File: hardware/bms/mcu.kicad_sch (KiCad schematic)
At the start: 34 parts

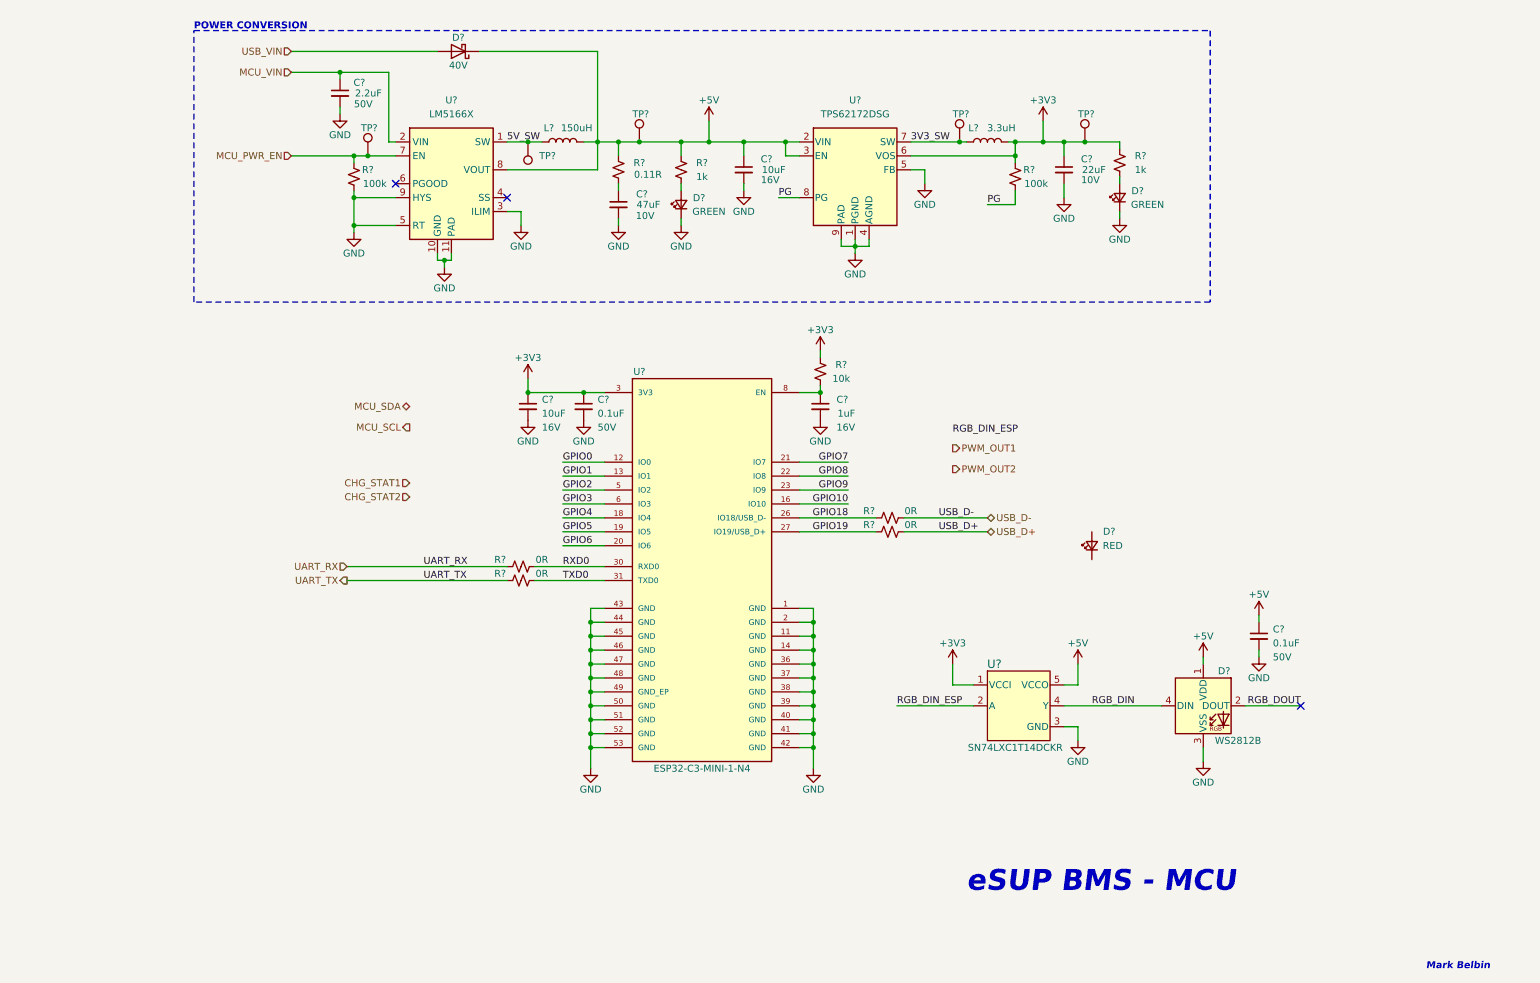
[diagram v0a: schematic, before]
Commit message: Sch mostly complete! Just have the USB C connector left to sort out.
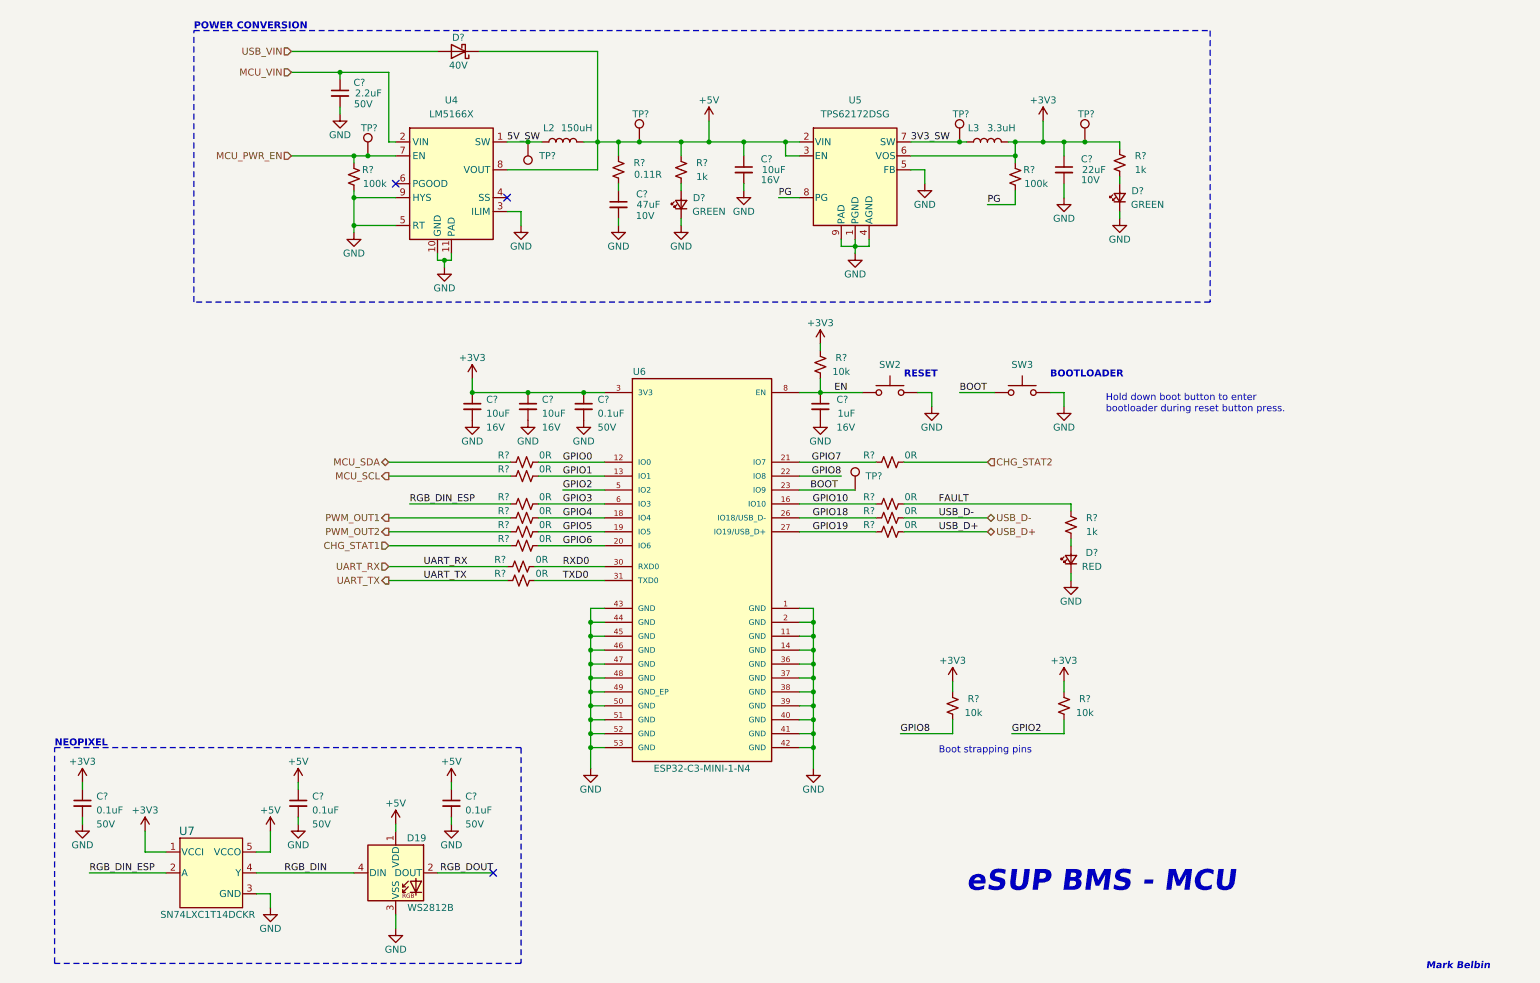
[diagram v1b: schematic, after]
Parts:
- added C? (x2): 0.1uF, Capacitor_SMD:C_0603_1608Metric, symbol Device:C_Small
- added C?: 10uF, Capacitor_SMD:C_0603_1608Metric, symbol Device:C_Small
- added R? (x2): 10k, Resistor_SMD:R_0603_1608Metric, symbol Device:R_Small_US
- added R? (x8): 0R, Resistor_SMD:R_0603_1608Metric, symbol Device:R_Small_US
- added R?: 1k, Resistor_SMD:R_0603_1608Metric, symbol Device:R_Small_US
- added SW2, SW3: SW_Push, bms:SW_B3U-1000P, symbol Switch:SW_Push
- added TP?: TestPoint, TestPoint:TestPoint_Pad_D1.0mm, symbol Connector:TestPoint
- L3: renamed from L?; footprint (none) -> Inductor_SMD:L_1008_2520Metric; Current (none) -> 1.2A; DCR (none) -> 125m; MFG (none) -> Murata Electronics; MFG PN (none) -> LQM2HPN3R3MG0L
- gave numbers to parts that had none: 6
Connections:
- net +3V3: now also C?.1, C?.1, R?.1, R?.1
- net +5V: now also C?.1
- net CHG_STAT1: now also R?.1
- net CHG_STAT2: now also R?.2
- net GND: now also D?.1 (K), C?.2, C?.2, C?.2, SW2.2, SW3.2
- net GPIO0: now also R?.2
- net GPIO1: now also R?.2
- net GPIO10: now also R?.1
- net GPIO2: now also R?.2
- net GPIO3: now also R?.2
- net GPIO4: now also R?.2
- net GPIO5: now also R?.2
- net GPIO6: now also R?.2
- net GPIO7: now also R?.1
- net GPIO8: now also R?.2
- net MCU_SCL: now also R?.1
- net MCU_SDA: now also R?.1
- net PWM_OUT1: now also R?.1
- net PWM_OUT2: now also R?.1
- net RGB_DIN_ESP: now also R?.1
- net at D?.2 (A): now also R?.1
- net EN: now reaches C?.1, R?.2, U6.8 (EN)
- net EN: now also SW2.1
- net GPIO9 renamed BOOT
- net BOOT: now also SW3.1, TP?.1
- new net FAULT: R?.2, R?.2
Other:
- note added: "BOOTLOADER"
- note added: "Boot strapping pins"
- note added: "Hold down boot button to enter bootloader during reset button press."
- note added: "NEOPIXEL"
- note added: "RESET"
- title: (none) -> eSUP - ESP32 MCU
- moved on the sheet: C?, D19, D?, R?, U7

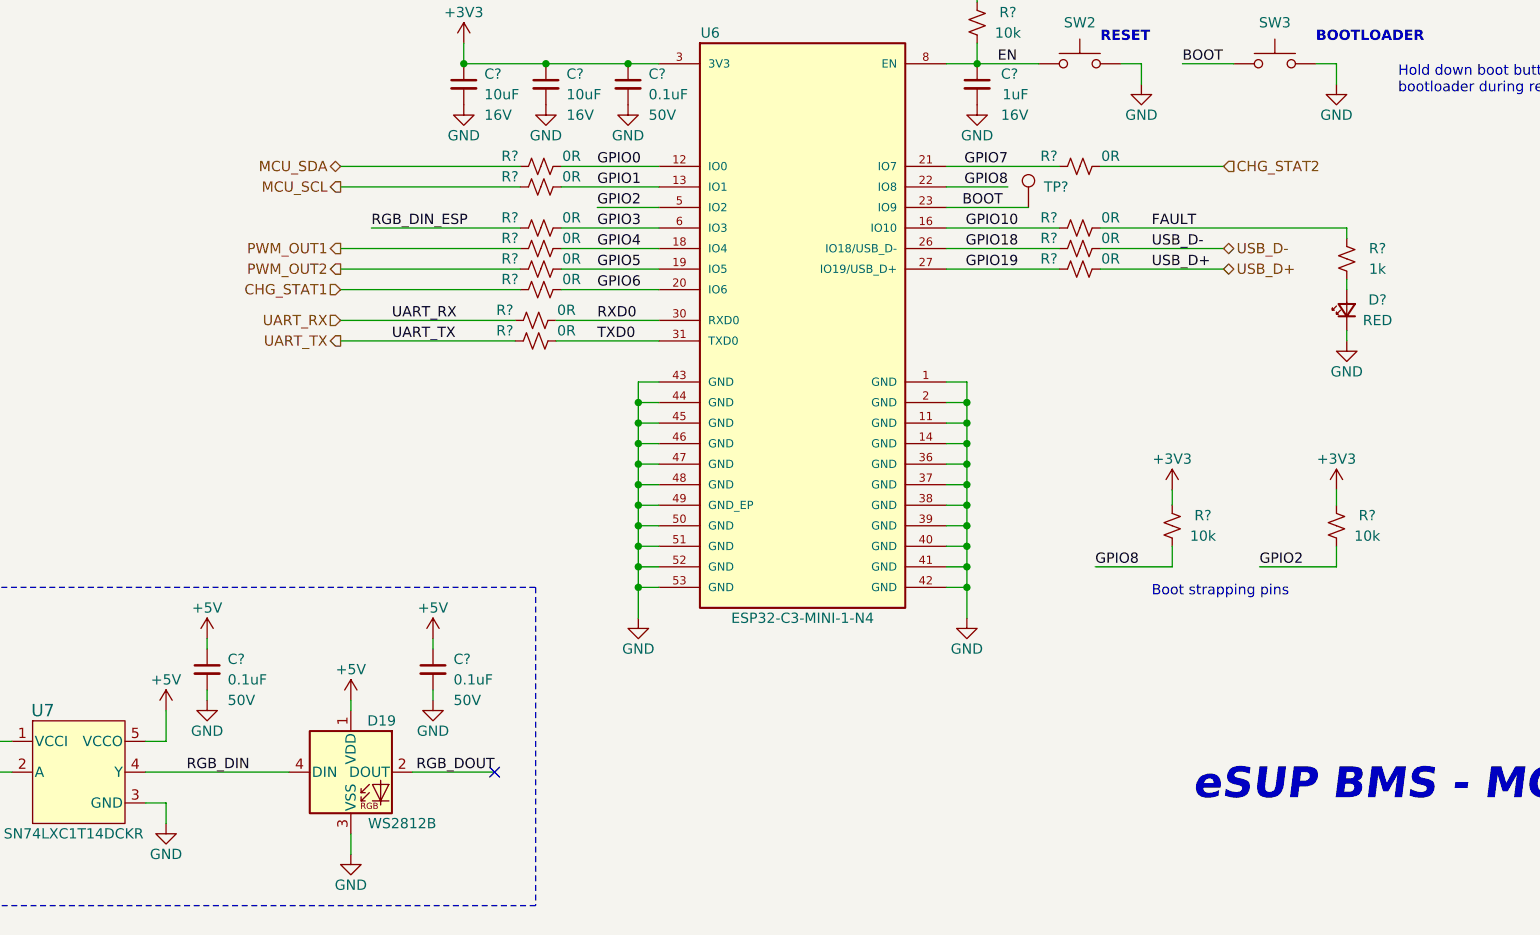
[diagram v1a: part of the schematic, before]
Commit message: Updated USB C connector, fixed all sch ERC errors, imported footprints into pcb file, fixed any pcb import errors.
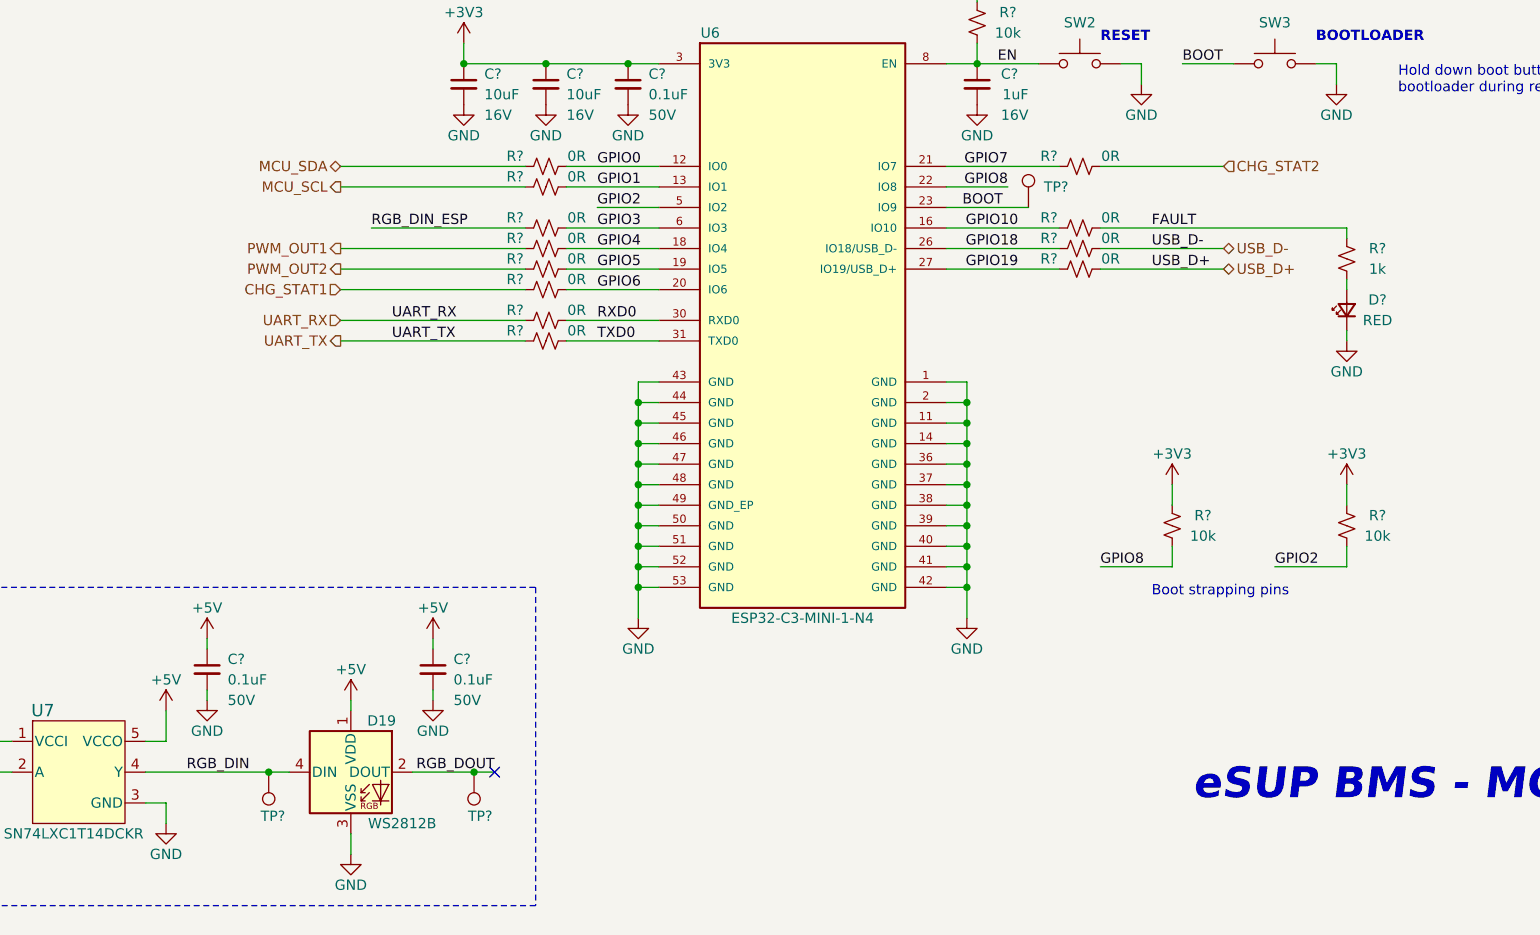
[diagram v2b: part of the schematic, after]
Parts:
- added TP? (x2): TestPoint, TestPoint:TestPoint_Pad_D1.0mm, symbol Connector:TestPoint
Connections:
- net RGB_DIN: now also TP?.1
- net RGB_DOUT: now also TP?.1
- now unconnected: U6.10 (NC), U6.15 (NC), U6.17 (NC), U6.24 (NC), U6.25 (NC), U6.28 (NC), U6.29 (NC), U6.32 (NC), U6.33 (NC), U6.34 (NC), U6.35 (NC), U6.4 (NC), U6.7 (NC), U6.9 (NC)
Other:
- moved on the sheet: R?

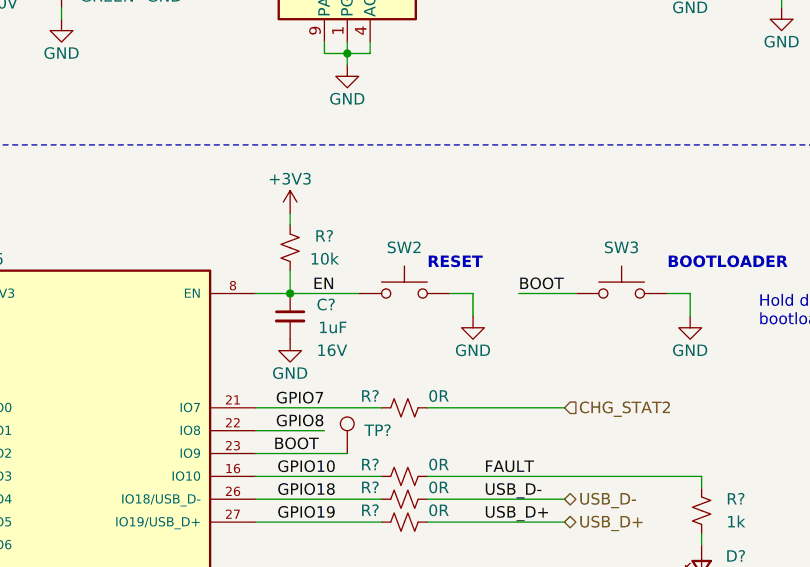
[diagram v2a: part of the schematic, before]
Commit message: Sch cleanup, added extra netties
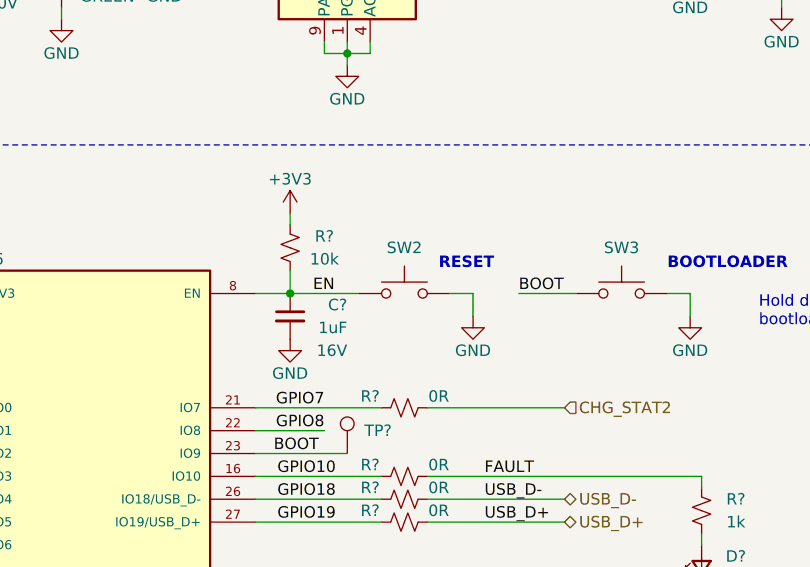
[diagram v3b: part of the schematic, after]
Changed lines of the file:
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@@
     (effects (font (size 1.27 1.27) (thickness 0.254) bold italic) (justify left bottom))
   )
-  (text "RESET" (at 176.53 82.55 0)
+  (text "RESET" (at 177.8 82.55 0)
     (effects (font (size 1.27 1.27) (thickness 0.254) bold) (justify left bottom))
   )
@@
   (symbol (lib_id "Device:C_Small") (at 161.29 87.63 0) (mirror y) (unit 1)
     (in_bom yes) (on_board yes) (dnp no)
-    (property "Reference" "C?" (at 166.37 86.36 0)
-      (effects (font (size 1.27 1.27)) (justify left))
-    )
+    (property "Reference" "C?" (at 167.64 86.36 0)
+      (effects (font (size 1.27 1.27)) (justify left))
+    )
